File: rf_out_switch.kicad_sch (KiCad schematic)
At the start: 9 parts, among them J11 Molex 73251-1153, J14 Molex 73251-1153, U33 QPC1022TR7, U34 QPC1022TR7

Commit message: Change transmit power dissipation resistors to 2W
Signed-off-by: Corey Minyard <corey@minyard.net>
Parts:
- R104, R109: value 50 -> 50R >=2W; footprint Resistor_SMD:R_0603_1608Metric_Pad0.98x0.95mm_HandSolder -> Resistor_SMD:R_1206_3216Metric_Pad1.30x1.75mm_HandSolder
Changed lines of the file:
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@@
 			)
 		)
-		(property "Value" "50"
-			(at 85.852 82.296 0)
+		(property "Value" "50R >=2W"
+			(at 78.74 76.708 90)
 			(effects
 				(font
@@
 			)
 		)
-		(property "Footprint" "Resistor_SMD:R_0603_1608Metric_Pad0.98x0.95mm_HandSolder"
+		(property "Footprint" "Resistor_SMD:R_1206_3216Metric_Pad1.30x1.75mm_HandSolder"
 			(at 79.502 81.28 90)
 			(effects
@@
 			)
 		)
-		(property "Value" "50"
-			(at 197.612 111.506 0)
+		(property "Value" "50R >=2W"
+			(at 195.834 110.998 90)
 			(effects
 				(font
@@
 			)
 		)
-		(property "Footprint" "Resistor_SMD:R_0603_1608Metric_Pad0.98x0.95mm_HandSolder"
+		(property "Footprint" "Resistor_SMD:R_1206_3216Metric_Pad1.30x1.75mm_HandSolder"
 			(at 191.262 110.49 90)
 			(effects

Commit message: Add an RF loopback test
Signed-off-by: Corey Minyard <corey@minyard.net>
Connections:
- net GND: no longer R104.2, R109.2
- new net BOARD1_RF_BYPASS: R104.2
- new net BOARD2_RF_BYPASS: R109.2
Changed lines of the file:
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@@
+	(wire
+		(pts
+			(xy 81.28 93.98) (xy 71.12 93.98)
+		)
+		(stroke
+			(width 0)
+			(type default)
+		)
+	)
+	(wire
+		(pts
+			(xy 81.28 85.09) (xy 81.28 93.98)
+		)
+		(stroke
+			(width 0)
+			(type default)
+		)
+	)
 	(wire
 		(pts
@@
 	(wire
 		(pts
+			(xy 193.04 114.3) (xy 193.04 125.73)
+		)
+		(stroke
+			(width 0)
+			(type default)
+		)
+	)
+	(wire
+		(pts
 			(xy 92.71 107.95) (xy 92.71 118.11)
 		)
@@
 	(wire
 		(pts
-			(xy 81.28 85.09) (xy 81.28 87.63)
-		)
-		(stroke
-			(width 0)
-			(type default)
-		)
-	)
-	(wire
-		(pts
 			(xy 85.09 143.51) (xy 85.09 146.05)
 		)
@@
 	(wire
 		(pts
-			(xy 193.04 114.3) (xy 193.04 116.84)
-		)
-		(stroke
-			(width 0)
-			(type default)
-		)
-	)
-	(wire
-		(pts
 			(xy 148.59 102.87) (xy 148.59 91.44)
 		)
@@
 		(pts
 			(xy 85.09 125.73) (xy 85.09 118.11)
+		)
+		(stroke
+			(width 0)
+			(type default)
+		)
+	)
+	(wire
+		(pts
+			(xy 193.04 125.73) (xy 207.01 125.73)
 		)
 		(stroke
@@
 		(property "Intersheetrefs" "${INTERSHEET_REFS}"
 			(at 156.3941 130.81 0)
+			(effects
+				(font
+					(size 1.27 1.27)
+				)
+				(justify left)
+				(hide yes)
+			)
+		)
+	)
+	(global_label "BOARD1_RF_BYPASS"
+		(shape input)
+		(at 71.12 93.98 180)
+		(fields_autoplaced yes)
+		(effects
+			(font
+				(size 1.524 1.524)
+			)
+			(justify right)
+		)
+		(property "Intersheetrefs" "${INTERSHEET_REFS}"
+			(at 45.681 93.98 0)
+			(effects
+				(font
+					(size 1.27 1.27)
+				)
+				(justify right)
+				(hide yes)
+			)
+		)
+	)
+	(global_label "BOARD2_RF_BYPASS"
+		(shape input)
+		(at 207.01 125.73 0)
+		(fields_autoplaced yes)
+		(effects
+			(font
+				(size 1.524 1.524)
+			)
+			(justify left)
+		)
+		(property "Intersheetrefs" "${INTERSHEET_REFS}"
+			(at 232.449 125.73 0)
 			(effects
 				(font
@@
 	(symbol
 		(lib_id "power:GND")
-		(at 193.04 116.84 0)
-		(unit 1)
-		(exclude_from_sim no)
-		(in_bom yes)
-		(on_board yes)
-		(dnp no)
-		(fields_autoplaced yes)
-		(property "Reference" "#PWR0285"
-			(at 193.04 123.19 0)
-			(effects
-				(font
-					(size 1.27 1.27)
-				)
-				(hide yes)
-			)
-		)
-		(property "Value" "GND"
-			(at 193.04 121.92 0)
-			(effects
-				(font
-					(size 1.27 1.27)
-				)
-			)
-		)
-		(property "Footprint" ""
-			(at 193.04 116.84 0)
-			(effects
-				(font
-					(size 1.27 1.27)
-				)
-				(hide yes)
-			)
-		)
-		(property "Datasheet" ""
-			(at 193.04 116.84 0)
-			(effects
-				(font
-					(size 1.27 1.27)
-				)
-				(hide yes)
-			)
-		)
-		(property "Description" ""
-			(at 193.04 116.84 0)
-			(effects
-				(font
-					(size 1.27 1.27)
-				)
-			)
-		)
-		(pin "1"
-		)
-		(instances
-			(project "PacSat_AFSK"
-				(path "/cc9f42d2-6985-41ac-acab-5ab7b01c5b38/4fa888af-703c-49ed-93bb-d56d2f02c470/26e0c845-9451-4c79-aef3-943c70af8ca9"
-					(reference "#PWR0285")
-					(unit 1)
-				)
-			)
-		)
-	)
-	(symbol
-		(lib_id "power:GND")
 		(at 140.97 74.93 0)
 		(unit 1)
@@
 					(unit 1)
 				)
-			)
-		)
-	)
-	(symbol
-		(lib_id "power:GND")
-		(at 81.28 87.63 0)
-		(unit 1)
-		(exclude_from_sim no)
-		(in_bom yes)
-		(on_board yes)
-		(dnp no)
-		(fields_autoplaced yes)
-		(property "Reference" "#PWR0234"
-			(at 81.28 93.98 0)
-			(effects
-				(font
-					(size 1.27 1.27)
-				)
-				(hide yes)
-			)
-		)
-		(property "Value" "GND"
-			(at 81.28 92.71 0)
-			(effects
-				(font
-					(size 1.27 1.27)
-				)
-			)
-		)
-		(property "Footprint" ""
-			(at 81.28 87.63 0)
-			(effects
-				(font
-					(size 1.27 1.27)
-				)
-				(hide yes)
-			)
-		)
-		(property "Datasheet" ""
-			(at 81.28 87.63 0)
-			(effects
-				(font
-					(size 1.27 1.27)
-				)
-				(hide yes)
-			)
-		)
-		(property "Description" ""
-			(at 81.28 87.63 0)
-			(effects
-				(font
-					(size 1.27 1.27)
-				)
-			)
-		)
-		(pin "1"
-		)
-		(instances
-			(project "PacSat_AFSK"
-				(path "/cc9f42d2-6985-41ac-acab-5ab7b01c5b38/4fa888af-703c-49ed-93bb-d56d2f02c470/26e0c845-9451-4c79-aef3-943c70af8ca9"
-					(reference "#PWR0234")
-					(unit 1)
-				)

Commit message: Move to vertical SMA connectors
Required quite a bit of rework.

Signed-off-by: Corey Minyard <corey@minyard.net>
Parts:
- J11, J14: value Molex 73251-1153 -> Wirth 60312002114503; footprint Connector_Coaxial:SMA_Molex_73251-1153_EdgeMount_Horizontal -> Connector_Coaxial:SMA_Wurth_60312002114503_Vertical
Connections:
- net RF_SWITCH_EN: now reaches R105.2, R106.1, U33.6 (EN), U34.6 (EN)

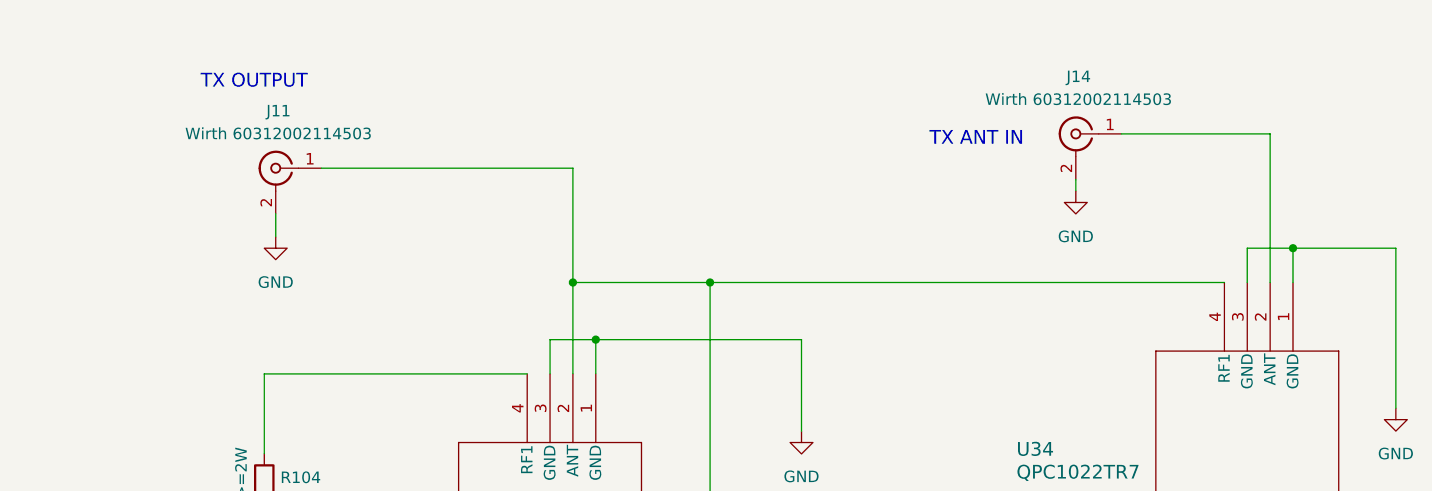
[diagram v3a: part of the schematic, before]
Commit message: Change RF connectors to U.FL
I'll solder a U.FL to SMA connector for testing.

Signed-off-by: Corey Minyard <corey@minyard.net>
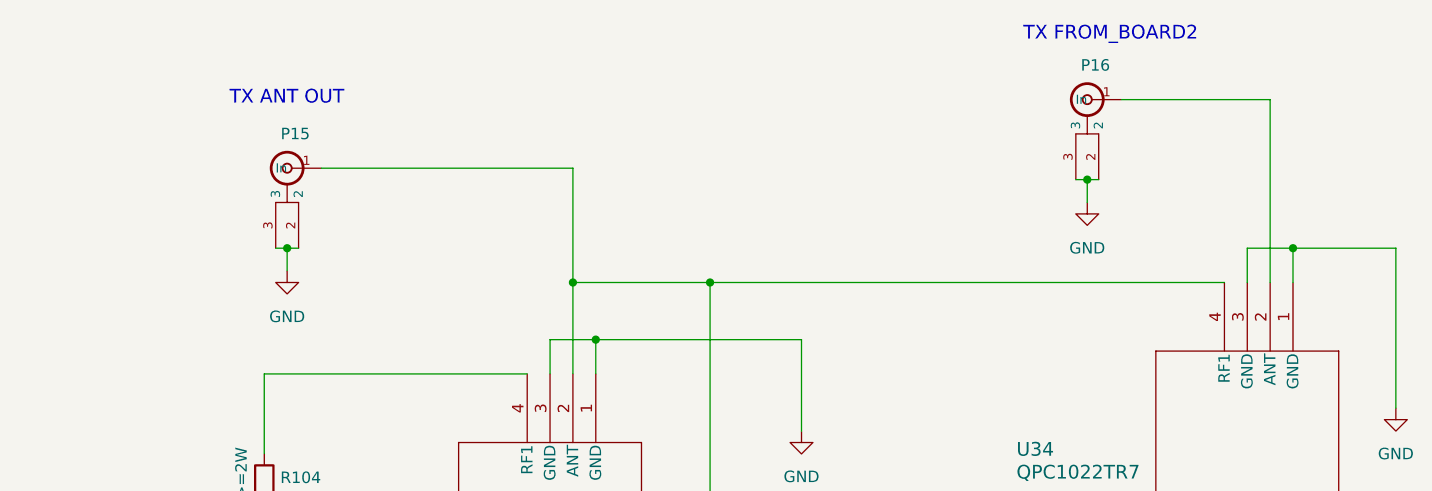
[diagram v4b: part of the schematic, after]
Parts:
- removed J11, J14: Wirth 60312002114503, Connector_Coaxial:SMA_Wurth_60312002114503_Vertical, symbol Connector:Conn_Coaxial
- added P15, P16: CONUFL001-SMD-T, PacSatDev_misc:CONN1_CONUFL_TEC, symbol PACSAT_DEV_misc:U_FL
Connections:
- net GND: now also P15.2, P15.3, P16.2, P16.3
- net at U34.2 (ANT): now also P16.1 (In)
- net at R107.1, U33.2 (ANT), U34.4 (RF1): now also P15.1 (In)
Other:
- note added: "TX ANT OUT"
- note added: "TX FROM_BOARD2"
- note removed: "TX ANT IN"
- note removed: "TX OUTPUT"

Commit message: Convert the LNA and PA portions to 0402
Where appropriate

Signed-off-by: Corey Minyard <corey@minyard.net>
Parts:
- R105, R106: footprint Resistor_SMD:R_0603_1608Metric_Pad0.98x0.95mm_HandSolder -> Resistor_SMD:R_0402_1005Metric_Pad0.72x0.64mm_HandSolder
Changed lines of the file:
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@@
 			)
 		)
-		(property "Footprint" "Resistor_SMD:R_0603_1608Metric_Pad0.98x0.95mm_HandSolder"
+		(property "Footprint" "Resistor_SMD:R_0402_1005Metric_Pad0.72x0.64mm_HandSolder"
 			(at 83.312 139.7 90)
 			(effects
@@
 			)
 		)
-		(property "Footprint" "Resistor_SMD:R_0603_1608Metric_Pad0.98x0.95mm_HandSolder"
+		(property "Footprint" "Resistor_SMD:R_0402_1005Metric_Pad0.72x0.64mm_HandSolder"
 			(at 83.312 129.54 90)
 			(effects

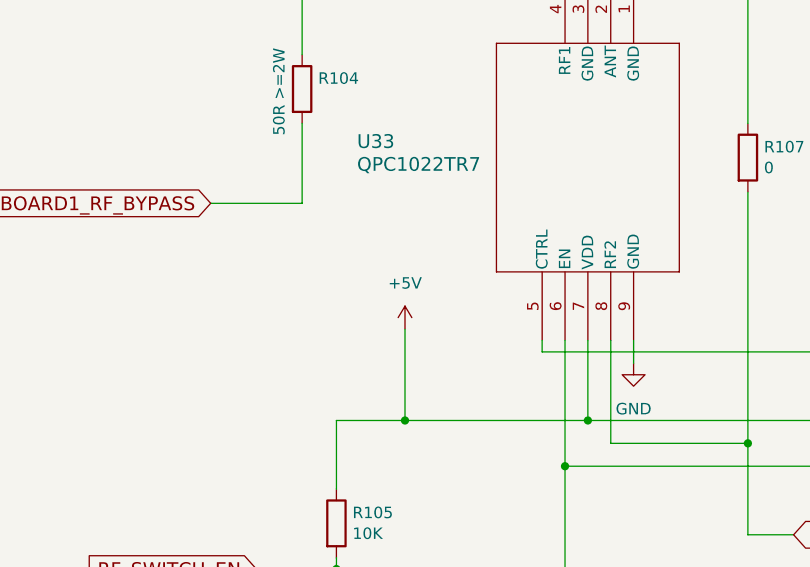
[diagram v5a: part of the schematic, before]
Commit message: Add a current limiter for on-board +5V devices
Signed-off-by: Corey Minyard <corey@minyard.net>
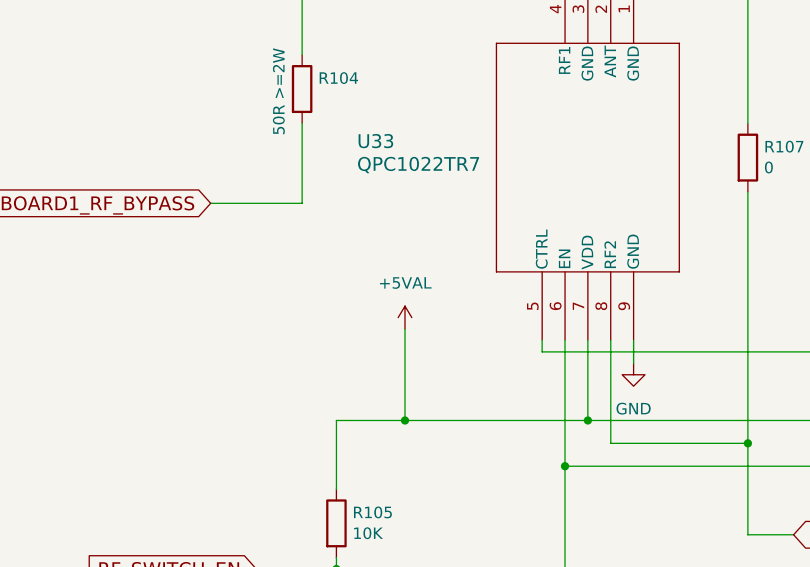
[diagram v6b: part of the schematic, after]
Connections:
- net +5V renamed +5VAL
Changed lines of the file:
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@@
 			)
 		)
-		(property "Value" "+5V"
+		(property "Value" "+5VAL"
 			(at 92.71 102.87 0)
 			(effects

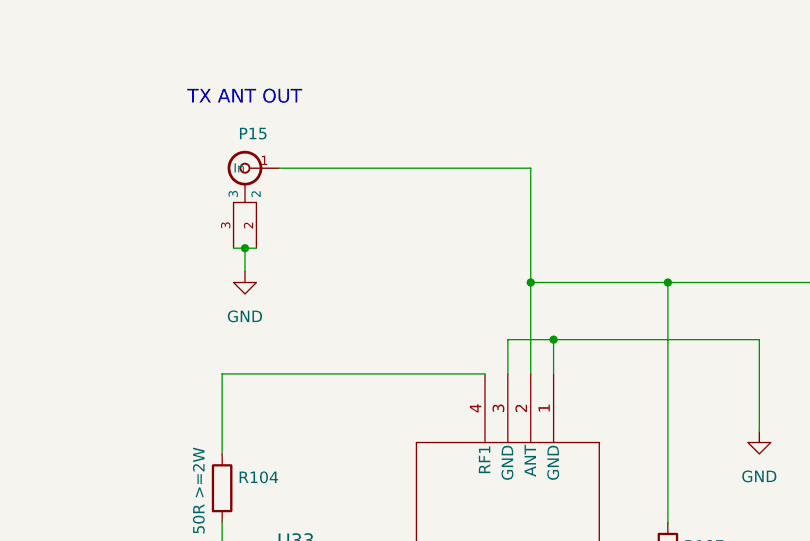
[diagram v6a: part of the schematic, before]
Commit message: Replace the output filter with a discrete one
The part chosen for the output filter didn't have very good ratings with
respect to being shaken and nothing on thermal cycles.  Also, it only
had 30dB of output filtering.  Replace with a discrete filter.

Signed-off-by: Corey Minyard <corey@minyard.net>
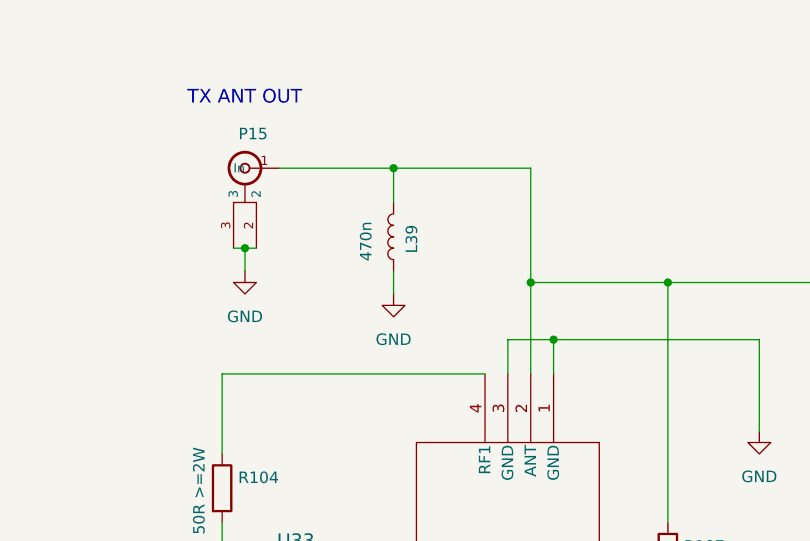
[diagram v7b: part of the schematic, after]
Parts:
- added L39: 470n, Inductor_SMD:L_0805_2012Metric_Pad1.05x1.20mm_HandSolder, symbol Device:L
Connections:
- net GND: now also L39.2
- net at P15.1 (In), R107.1, U33.2 (ANT)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: now also L39.1
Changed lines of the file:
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@@
+	)
+	(junction
+		(at 100.33 45.72)
+		(diameter 0)
+		(color 0 0 0 0)
 	)
 	(junction
@@
 	(wire
 		(pts
+			(xy 100.33 45.72) (xy 115.57 45.72)
+		)
+		(stroke
+			(width 0)
+			(type default)
+		)
+	)
+	(wire
+		(pts
 			(xy 130.81 58.42) (xy 187.96 58.42)
 		)
@@
 	(wire
 		(pts
-			(xy 87.63 45.72) (xy 115.57 45.72)
+			(xy 87.63 45.72) (xy 100.33 45.72)
 		)
 		(stroke
@@
 	(wire
 		(pts
+			(xy 100.33 57.15) (xy 100.33 59.69)
+		)
+		(stroke
+			(width 0)
+			(type default)
+		)
+	)
+	(wire
+		(pts
 			(xy 81.28 68.58) (xy 110.49 68.58)
 		)
@@
 		(pts
 			(xy 193.04 125.73) (xy 207.01 125.73)
+		)
+		(stroke
+			(width 0)
+			(type default)
+		)
+	)
+	(wire
+		(pts
+			(xy 100.33 45.72) (xy 100.33 49.53)
 		)
 		(stroke
@@
 	)
 	(symbol
+		(lib_id "Device:L")
+		(at 100.33 53.34 0)
+		(mirror y)
+		(unit 1)
+		(exclude_from_sim no)
+		(in_bom yes)
+		(on_board yes)
+		(dnp no)
+		(property "Reference" "L39"
+			(at 102.362 53.594 90)
+			(effects
+				(font
+					(size 1.27 1.27)
+				)
+			)
+		)
+		(property "Value" "470n"
+			(at 97.282 53.848 90)
+			(effects
+				(font
+					(size 1.27 1.27)
+				)
+			)
+		)
+		(property "Footprint" "Inductor_SMD:L_0805_2012Metric_Pad1.05x1.20mm_HandSolder"
+			(at 100.33 53.34 0)
+			(effects
+				(font
+					(size 1.27 1.27)
+				)
+				(hide yes)
+			)
+		)
+		(property "Datasheet" "~"
+			(at 100.33 53.34 0)
+			(effects
+				(font
+					(size 1.27 1.27)
+				)
+				(hide yes)
+			)
+		)
+		(property "Description" ""
+			(at 100.33 53.34 0)
+			(effects
+				(font
+					(size 1.27 1.27)
+				)
+			)
+		)
+		(pin "1"
+		)
+		(pin "2"
+		)
+		(instances
+			(project "PacSat_AFSK"
+				(path "/cc9f42d2-6985-41ac-acab-5ab7b01c5b38/4fa888af-703c-49ed-93bb-d56d2f02c470/26e0c845-9451-4c79-aef3-943c70af8ca9"
+					(reference "L39")
+					(unit 1)
+				)
+			)
+		)
+	)
+	(symbol
 		(lib_id "power:+5V")
 		(at 92.71 107.95 0)
@@
 					(unit 1)
 				)
+			)
+		)
+	)
+	(symbol
+		(lib_id "power:GND")
+		(at 100.33 59.69 0)
+		(unit 1)
+		(exclude_from_sim no)
+		(in_bom yes)
+		(on_board yes)
+		(dnp no)
+		(fields_autoplaced yes)
+		(property "Reference" "#PWR0292"
+			(at 100.33 66.04 0)
+			(effects
+				(font
+					(size 1.27 1.27)
+				)
+				(hide yes)
+			)
+		)
+		(property "Value" "GND"
+			(at 100.33 64.77 0)
+			(effects
+				(font
+					(size 1.27 1.27)
+				)
+			)
+		)
+		(property "Footprint" ""
+			(at 100.33 59.69 0)
+			(effects
+				(font
+					(size 1.27 1.27)
+				)
+				(hide yes)
+			)
+		)
+		(property "Datasheet" ""
+			(at 100.33 59.69 0)
+			(effects
+				(font
+					(size 1.27 1.27)
+				)
+				(hide yes)
+			)
+		)
+		(property "Description" ""
+			(at 100.33 59.69 0)
+			(effects
+				(font
+					(size 1.27 1.27)
+				)
+			)
+		)
+		(pin "1"
+		)
+		(instances
+			(project "PacSat_AFSK"
+				(path "/cc9f42d2-6985-41ac-acab-5ab7b01c5b38/4fa888af-703c-49ed-93bb-d56d2f02c470/26e0c845-9451-4c79-aef3-943c70af8ca9"
+					(reference "#PWR0292")
+					(unit 1)
+				)

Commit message: Fix some notes
Signed-off-by: Corey Minyard <corey@minyard.net>
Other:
- note added: "Inductor to bleed off static build up on the antenna."
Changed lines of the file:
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@@
+		)
+	)
+	(text "Inductor to bleed off static build\nup on the antenna."
+		(exclude_from_sim no)
+		(at 115.57 42.672 0)
+		(effects
+			(font
+				(size 1.524 1.524)
+			)
 		)
 	)
